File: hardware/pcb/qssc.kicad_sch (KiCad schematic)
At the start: 126 parts, among them J1 FT232RL, J10 USB-C, J12 BTB_HOST, J2 5V Barrel, J3 SMA, J4 12V LED, J7 RESET, J8 MW_GATE, J9 JTAG, U1 XC7A35T-1CSG324C, U3 ADF4351BCPZ, U5 GVA-84+, U8 W25Q128JVSIQ, Y1 100MHz TCXO

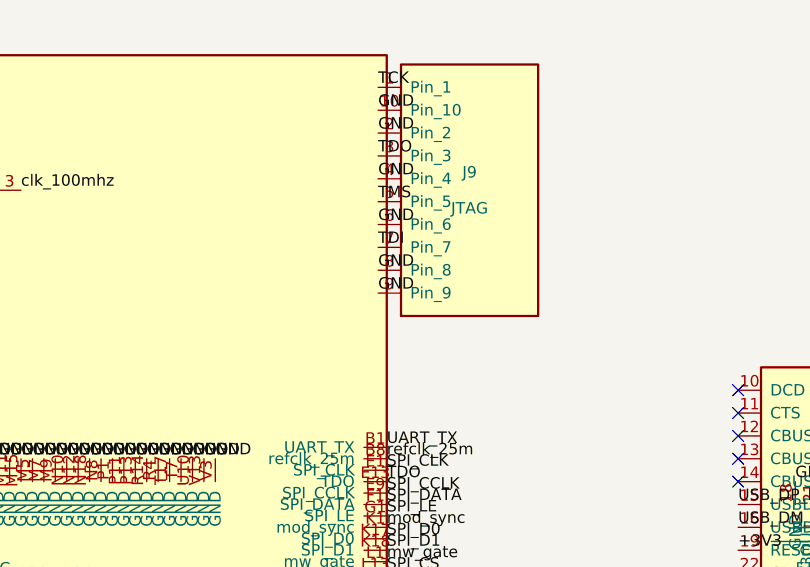
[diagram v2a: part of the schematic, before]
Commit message: head: bump detector head to 6 layers (4 signal layers for the die bus)
The 4-layer head put the 64-net die bus (DET_IN + DET_TIA) on only 2 signal
layers (F.Cu/B.Cu), at the autorouter's density ceiling.  6 layers add
In3.Cu + In4.Cu signal layers so route_signals + FreeRouting have 4 signal
layers (F.Cu/In3.Cu/In4.Cu/B.Cu).  route_signals.build() auto-selects the
4-signal-layer set from GetCopperLayerCount() (>4 branch), no router edit
needed; route_qssc_pcb reads plane labels dynamically.  HEAD_STACK_UP is a
6-layer 1.6mm FR4 build (In1.Cu GND one 0.15mm prepreg below F.Cu for the
TIA->ADC analog reference).  Die Uchip 64 DET pads stay on B.Cu.

Main board (qssc.*) is regenerated too: the JTAG J9 pin-9 +3V3 (VREF) fix
now comes from the generator code (replacing the earlier surgical edit),
and the .kicad_pcb is re-serialised in generator format (cosmetic
normalisation -- no layout/net change).  ruff CI rule clean.

Co-Authored-By: Claude Code <noreply@anthropic.com>
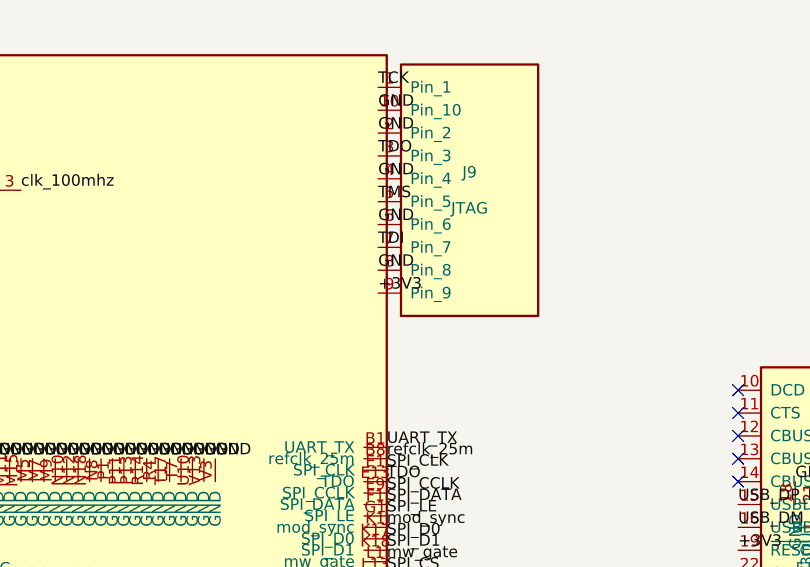
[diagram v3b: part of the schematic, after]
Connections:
- net +3V3: now also J9.9 (Pin_9)
- net GND: no longer J9.9 (Pin_9)
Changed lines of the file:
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@@
 		)
 	)
-	(label "GND"
+	(label "+3V3"
 		(at 249.84 41.43 0)
 		(fields_autoplaced yes)

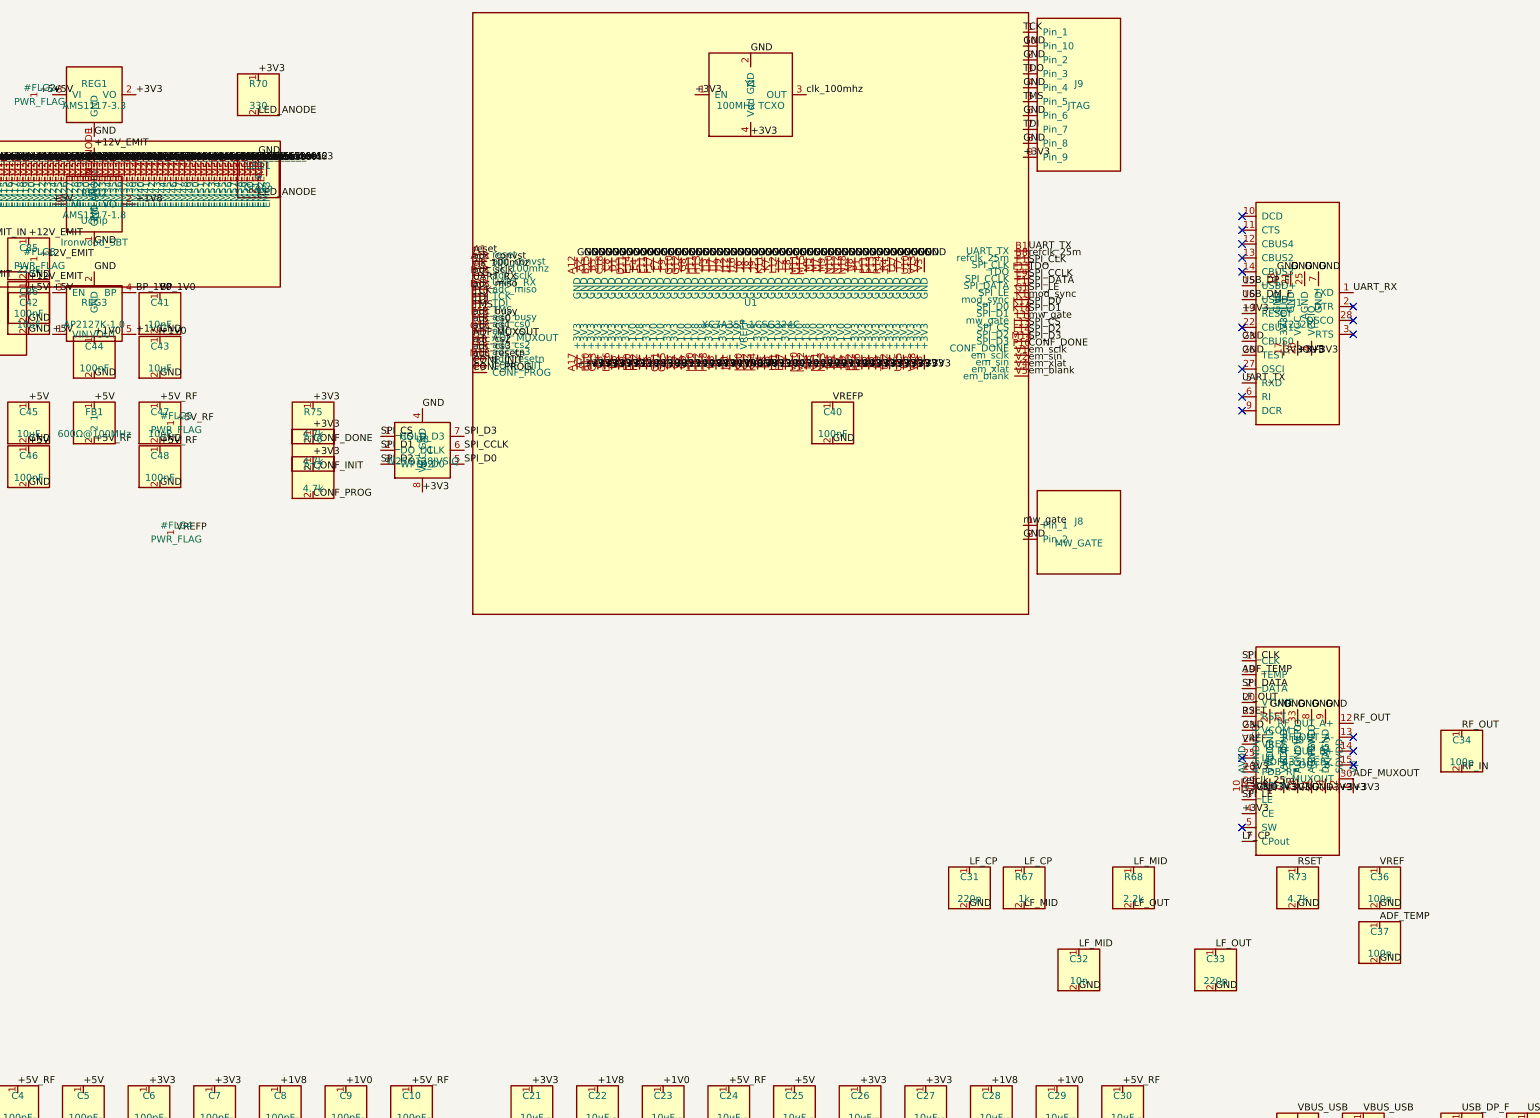
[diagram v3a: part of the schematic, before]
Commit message: pins: per-datasheet fixes (ADF4351 VCOM, FT232 CBUS0/NC, AP2127K pin4) + FPGA clock on P-side MRCC
Per-datasheet verification of all 11 components (real PDFs / KiCad symbols /
manufacturer datasheets) found 4 confirmed pin defects, now fixed:

- ADF4351 pin 23 (VCOM, internal compensation node biased at half the tuning
  range) was tied direct to GND -- shorting the half-range bias. Now decoupled
  to GND via a 100nF cap on a dedicated ADF_VCOM net (mirrors VREF/C36 and
  TEMP/C37). Verified from ADF4351.pdf p8 Pin Function table.
- FT232RL pin 23 is CBUS0 (not AGND); pin 24 is NC (not a 2nd VCC pad). The
  prior 'fix' tied 23->GND and 24->+3V3 under a wrong pin belief. Now both are
  no_connect; the real AGND is pin 25 (already GND). TXD/RXD comment labels
  corrected (nets are named from the FPGA side); 3V3OUT decoupler is C55 not C57.
  Verified from the KiCad Interface_USB:FT232RL symbol (omits NC pads 8 & 24).
- AP2127K-1.0 (REG3) fixed-output pin 4 is NC, not BP -- the prior C41 10nF
  tied a cap to a floating NC pad. Pin 4 -> no_connect; C41 designator reused
  for the ADF4351 VCOM decoupling cap. Noise reduction is via CIN/COUT
  (C42/C43/C44). Verified from Diodes AP2127K DS36478.
- FPGA clk_100mhz was on the N-side MRCC (A8), forcing a CLOCK_DEDICATED_ROUTE
  FALSE workaround (fabric routing, higher jitter). gen_fpga_ballmap_csg324.py
  now puts the input clock on the P-side MRCC (B8, dedicated delay-compensated
  route) and refclk_out on the N-side (A8); the XDC workaround is removed.
  Per UG472. Stale 'A14' doc references for refclk_25m corrected.

Label: the Abracon ASE 100 MHz oscillator is an XO (not a TCXO); schematic/BOM
value and comments corrected. Boards regenerated (both boards pick up the
ballmap swap + shared symbol-lib changes). HARDWARE_DESIGN.md pin-audit table
rows for FT232RL and ADF4351 corrected.

Co-Authored-By: Claude Code <noreply@anthropic.com>
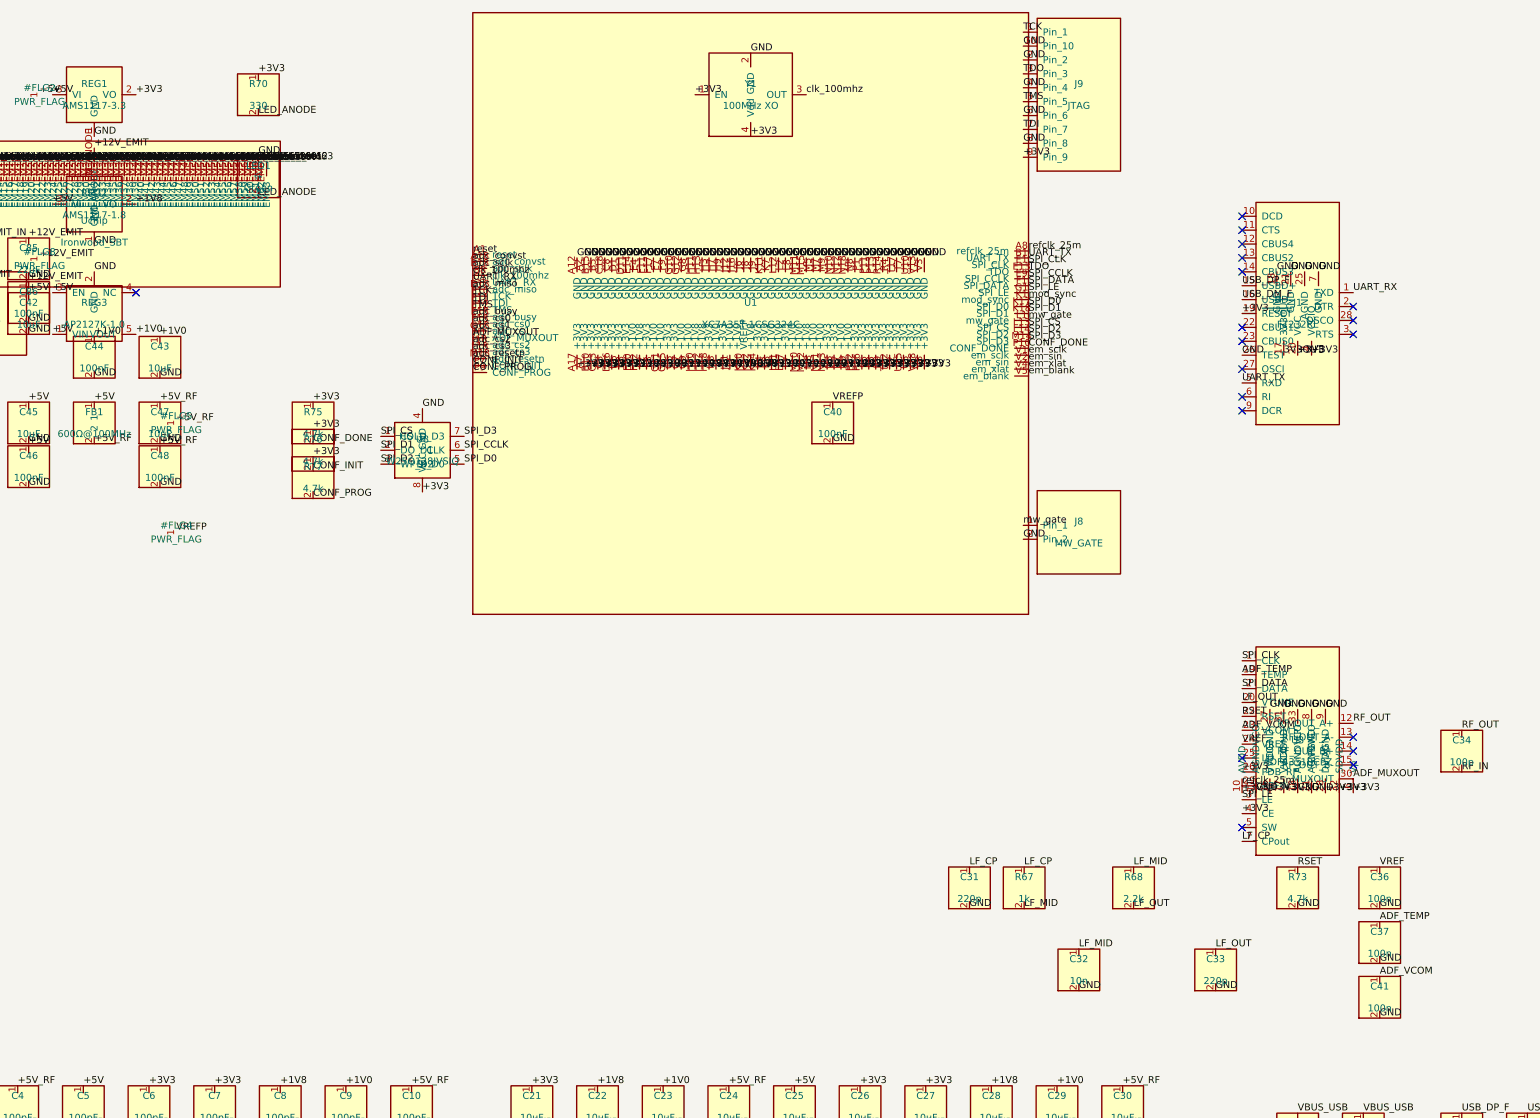
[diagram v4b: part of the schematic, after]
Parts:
- C41: value 10nF -> 100n
- Y1: value 100MHz TCXO -> 100MHz XO
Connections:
- net GND: no longer J1.23 (CBUS0), U3.23 (VCOM)
- net clk_100mhz: now also U1.B8 (clk_100mhz); no longer U1.A8 (clk_100mhz)
- net refclk_25m: now also U1.A8 (refclk_25m); no longer U1.B8 (refclk_25m)
- net BP_1V0: no longer names the net of REG3.4 (NC)
- net BP_1V0: no longer C41.1
- new net ADF_VCOM: C41.1, U3.23 (VCOM)
- no-connect marks 26 -> 28
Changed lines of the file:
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@@
 	(symbol
 		(lib_id "qssc:C")
-		(at 92 70 0)
-		(unit 1)
-		(exclude_from_sim no)
-		(in_bom yes)
-		(on_board yes)
-		(dnp no)
-		(property "Reference" "C41"
-			(at 92 68 0)
-			(effects
-				(font
-					(size 1.27 1.27)
-				)
-			)
-		)
-		(property "Value" "10nF"
-			(at 92 72 0)
-			(effects
-				(font
-					(size 1.27 1.27)
-				)
-			)
-		)
-		(property "Footprint" "Capacitor_SMD:C_0603_1608Metric"
-			(at 92 70 0)
-			(effects
-				(font
-					(size 1.27 1.27)
-				)
-				(hide yes)
-			)
-		)
-		(pin "1"
-		)
-		(pin "2"
-		)
-		(instances
-			(project "qssc"
-				(path "/00000000-0000-0000-0000-000000000001"
-					(reference "C41")
-					(unit 1)
-				)
-			)
-		)
-	)
-	(symbol
-		(lib_id "qssc:C")
 		(at 68 70 0)
 		(unit 1)
@@
 		(pin "A18"
 		)
-		(pin "A8"
-		)
 		(pin "B18"
 		)
+		(pin "B8"
+		)
 		(pin "C1"
 		)
@@
 		(pin "P9"
 		)
-		(pin "B1"
+		(pin "A8"
 		)
-		(pin "B8"
+		(pin "B1"
 		)
 		(pin "E1"
@@
 			)
 		)
-		(property "Value" "100MHz TCXO"
+		(property "Value" "100MHz XO"
 			(at 200 32 0)
 			(effects
@@
 	(symbol
 		(lib_id "qssc:C")
+		(at 315 195 0)
+		(unit 1)
+		(exclude_from_sim no)
+		(in_bom yes)
+		(on_board yes)
+		(dnp no)
+		(property "Reference" "C41"
+			(at 315 193 0)
+			(effects
+				(font
+					(size 1.27 1.27)
+				)
+			)
+		)
+		(property "Value" "100n"
+			(at 315 197 0)
+			(effects
+				(font
+					(size 1.27 1.27)
+				)
+			)
+		)
+		(property "Footprint" "Capacitor_SMD:C_0603_1608Metric"
+			(at 315 195 0)
+			(effects
+				(font
+					(size 1.27 1.27)
+				)
+				(hide yes)
+			)
+		)
+		(pin "1"
+		)
+		(pin "2"
+		)
+		(instances
+			(project "qssc"
+				(path "/00000000-0000-0000-0000-000000000001"
+					(reference "C41")
+					(unit 1)
+				)
+			)
+		)
+	)
+	(symbol
+		(lib_id "qssc:C")
 		(at 330 150 0)
 		(unit 1)
@@
 		)
 	)
-	(label "BP_1V0"
-		(at 87.62 66.19 0)
-		(fields_autoplaced yes)
-		(effects
-			(font
-				(size 1.27 1.27)
-			)
-			(justify left bottom)
-		)
-	)
 	(label "+1V0"
 		(at 87.62 73.81 0)
@@
 		)
 	)
-	(label "BP_1V0"
-		(at 92.0 66.19 0)
-		(fields_autoplaced yes)
-		(effects
-			(font
-				(size 1.27 1.27)
-			)
-			(justify left bottom)
-		)
-	)
-	(label "GND"
-		(at 92.0 73.81 0)
-		(fields_autoplaced yes)
-		(effects
-			(font
-				(size 1.27 1.27)
-			)
-			(justify left bottom)
-		)
-	)
 	(label "+5V"
 		(at 68.0 66.19 0)
@@
 	)
 	(label "adc_sclk"
-		(at 149.2 63.02 0)
+		(at 149.2 61.75 0)
 		(fields_autoplaced yes)
 		(effects
@@
 	)
 	(label "clk_100mhz"
-		(at 149.2 61.75 0)
+		(at 149.2 63.02 0)
 		(fields_autoplaced yes)
 		(effects
@@
 	)
 	(label "refclk_25m"
-		(at 250.8 59.84 0)
+		(at 250.8 58.57 0)
 		(fields_autoplaced yes)
 		(effects
@@
 	)
 	(label "UART_TX"
-		(at 250.8 58.57 0)
+		(at 250.8 59.84 0)
 		(fields_autoplaced yes)
 		(effects
@@
 	)
 	(label "GND"
-		(at 289.84 75.08 0)
-		(fields_autoplaced yes)
-		(effects
-			(font
-				(size 1.27 1.27)
-			)
-			(justify left bottom)
-		)
-	)
-	(label "GND"
 		(at 303.81 62.38 0)
 		(fields_autoplaced yes)
@@
 		)
 	)
-	(label "GND"
+	(label "ADF_VCOM"
 		(at 289.84 146.19 0)
 		(fields_autoplaced yes)
@@
 		)
 	)
+	(label "ADF_VCOM"
+		(at 315.0 191.19 0)
+		(fields_autoplaced yes)
+		(effects
+			(font
+				(size 1.27 1.27)
+			)
+			(justify left bottom)
+		)
+	)
+	(label "GND"
+		(at 315.0 198.81 0)
+		(fields_autoplaced yes)
+		(effects
+			(font
+				(size 1.27 1.27)
+			)
+			(justify left bottom)
+		)
+	)
 	(label "RF_OUT"
 		(at 330.0 146.19 0)
@@
 	)
 	(no_connect
+		(at 87.62 66.19)
+	)
+	(no_connect
 		(at 310.16 68.73)
 	)
@@
 	)
 	(no_connect
+		(at 289.84 75.08)
+	)
+	(no_connect

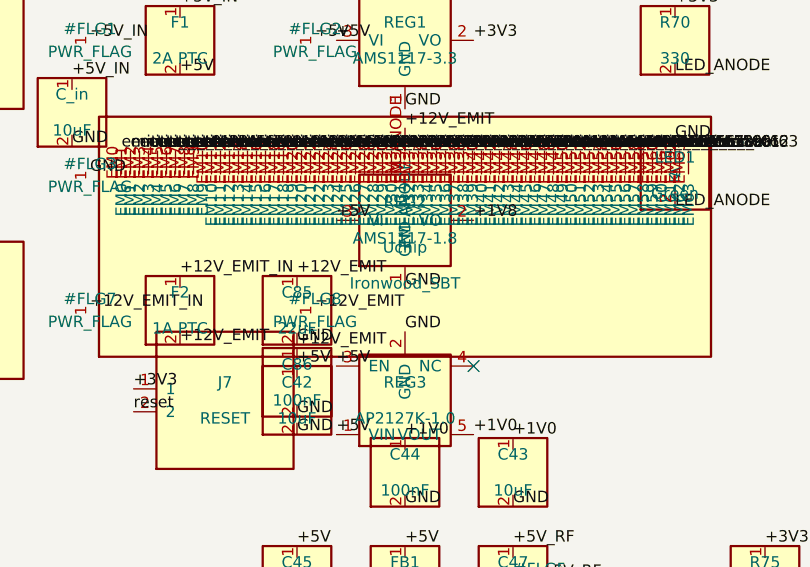
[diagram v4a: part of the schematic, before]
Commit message: pcb/main: route to perfection -- DRC 0/0/0 + 0 split/0 dangling
Main board fully routed with the user's back-ported component placement:

- DRC: 0 violations, 0 unconnected items (kicad-cli)
- Connectivity: 0 split nets, 0 dangling non-plane nets (test_pcb_connectivity)
- Full pytest suite green (202 passed, 9 skipped), exit 0
- 1780 tracks / 844 vias

USB-C reversible tie (tools/usb_c_reversible_tie.py, new): FreeRouting
routes one side of each D+/D- pair and leaves the other pad isolated -- the
0.5 mm USB-C pad field blocks any same-row tie (A6--B6 crosses A7 = D-,
shorting D+ to D-).  F.Cu is boxed in (inward = opposite-pair escapes +
vias; outward = VBUS_USB rail), so the tie is a 0.20/0.10 mm through
via-in-pad at the isolated pad + an L-track on In1.Cu to the partner's
trunk via.  route_qssc_pcb re-pours the GND plane afterwards, carving
clearance around the new via + track (no short to GND).  Idempotent.

BGA fanout root-cause fix (route_signals.py, committed d830e09): VIP every
signal ball + keep all unrouted VIPs through build() so FreeRouting always
has a via.  tools/bga_fanout_fix.py (post-hoc via adder, shorted rails)
removed -- superseded by the clean VIP-first re-route.

NO push: board perfect locally per user constraint; head board pending.

Co-Authored-By: Claude Code <noreply@anthropic.com>
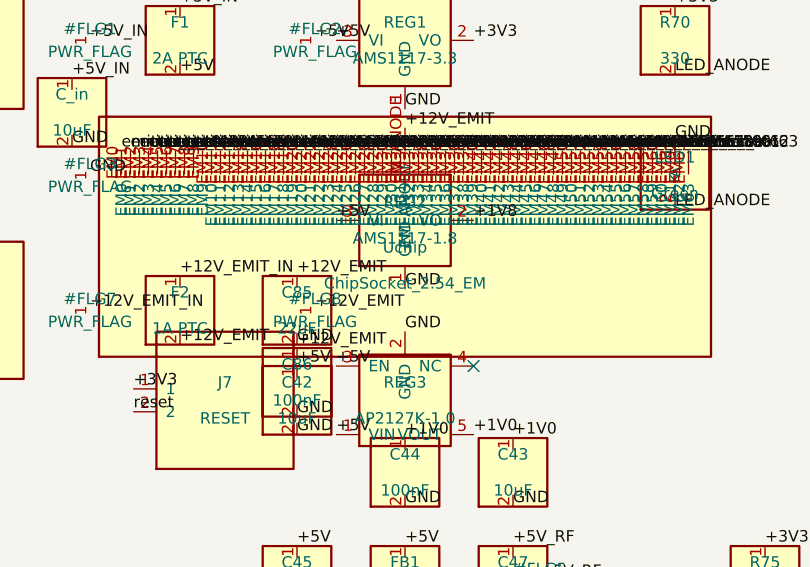
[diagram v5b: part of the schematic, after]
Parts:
- removed Uchip: Ironwood_SBT, qssc:Ironwood_SBT, symbol qssc:Ironwood_SBT
- added Uchip: ChipSocket_2.54_EM, qssc:ChipSocket_2.54_EM, symbol qssc:ChipSocket_2.54_EM
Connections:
- net +12V_EMIT: now also Uchip.EM_ANODE
- net emitter_cat0: now also Uchip.EM0
- net emitter_cat1: now also Uchip.EM1
- net emitter_cat10: now also Uchip.EM10
- net emitter_cat11: now also Uchip.EM11
- net emitter_cat12: now also Uchip.EM12
- net emitter_cat13: now also Uchip.EM13
- net emitter_cat14: now also Uchip.EM14
- net emitter_cat15: now also Uchip.EM15
- net emitter_cat16: now also Uchip.EM16
- net emitter_cat17: now also Uchip.EM17
- net emitter_cat18: now also Uchip.EM18
- net emitter_cat19: now also Uchip.EM19
- net emitter_cat2: now also Uchip.EM2
- net emitter_cat20: now also Uchip.EM20
- net emitter_cat21: now also Uchip.EM21
- net emitter_cat22: now also Uchip.EM22
- net emitter_cat23: now also Uchip.EM23
- net emitter_cat24: now also Uchip.EM24
- net emitter_cat25: now also Uchip.EM25
- net emitter_cat26: now also Uchip.EM26
- net emitter_cat27: now also Uchip.EM27
- net emitter_cat28: now also Uchip.EM28
- net emitter_cat29: now also Uchip.EM29
- net emitter_cat3: now also Uchip.EM3
- net emitter_cat30: now also Uchip.EM30
- net emitter_cat31: now also Uchip.EM31
- net emitter_cat32: now also Uchip.EM32
- net emitter_cat33: now also Uchip.EM33
- net emitter_cat34: now also Uchip.EM34
- net emitter_cat35: now also Uchip.EM35
- net emitter_cat36: now also Uchip.EM36
- net emitter_cat37: now also Uchip.EM37
- net emitter_cat38: now also Uchip.EM38
- net emitter_cat39: now also Uchip.EM39
- net emitter_cat4: now also Uchip.EM4
- net emitter_cat40: now also Uchip.EM40
- net emitter_cat41: now also Uchip.EM41
- net emitter_cat42: now also Uchip.EM42
- net emitter_cat43: now also Uchip.EM43
- net emitter_cat44: now also Uchip.EM44
- net emitter_cat45: now also Uchip.EM45
- net emitter_cat46: now also Uchip.EM46
- net emitter_cat47: now also Uchip.EM47
- net emitter_cat48: now also Uchip.EM48
- net emitter_cat49: now also Uchip.EM49
- net emitter_cat5: now also Uchip.EM5
- net emitter_cat50: now also Uchip.EM50
- net emitter_cat51: now also Uchip.EM51
- net emitter_cat52: now also Uchip.EM52
- net emitter_cat53: now also Uchip.EM53
- net emitter_cat54: now also Uchip.EM54
- net emitter_cat55: now also Uchip.EM55
- net emitter_cat56: now also Uchip.EM56
- net emitter_cat57: now also Uchip.EM57
- net emitter_cat58: now also Uchip.EM58
- net emitter_cat59: now also Uchip.EM59
- net emitter_cat6: now also Uchip.EM6
- net emitter_cat60: now also Uchip.EM60
- net emitter_cat61: now also Uchip.EM61
- net emitter_cat62: now also Uchip.EM62
- net emitter_cat63: now also Uchip.EM63
- net emitter_cat7: now also Uchip.EM7
- net emitter_cat8: now also Uchip.EM8
- net emitter_cat9: now also Uchip.EM9
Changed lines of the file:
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@@
 	)
 	(symbol
-		(lib_id "qssc:Ironwood_SBT")
+		(lib_id "qssc:ChipSocket_2.54_EM")
 		(at 80 55 0)
 		(unit 1)
@@
 			)
 		)
-		(property "Value" "Ironwood_SBT"
+		(property "Value" "ChipSocket_2.54_EM"
 			(at 80 57 0)
 			(effects
@@
 			)
 		)
-		(property "Footprint" "qssc:Ironwood_SBT"
+		(property "Footprint" "qssc:ChipSocket_2.54_EM"
 			(at 80 55 0)
 			(effects
